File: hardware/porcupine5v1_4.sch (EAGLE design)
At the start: 45 parts, among them X1 PROGCON

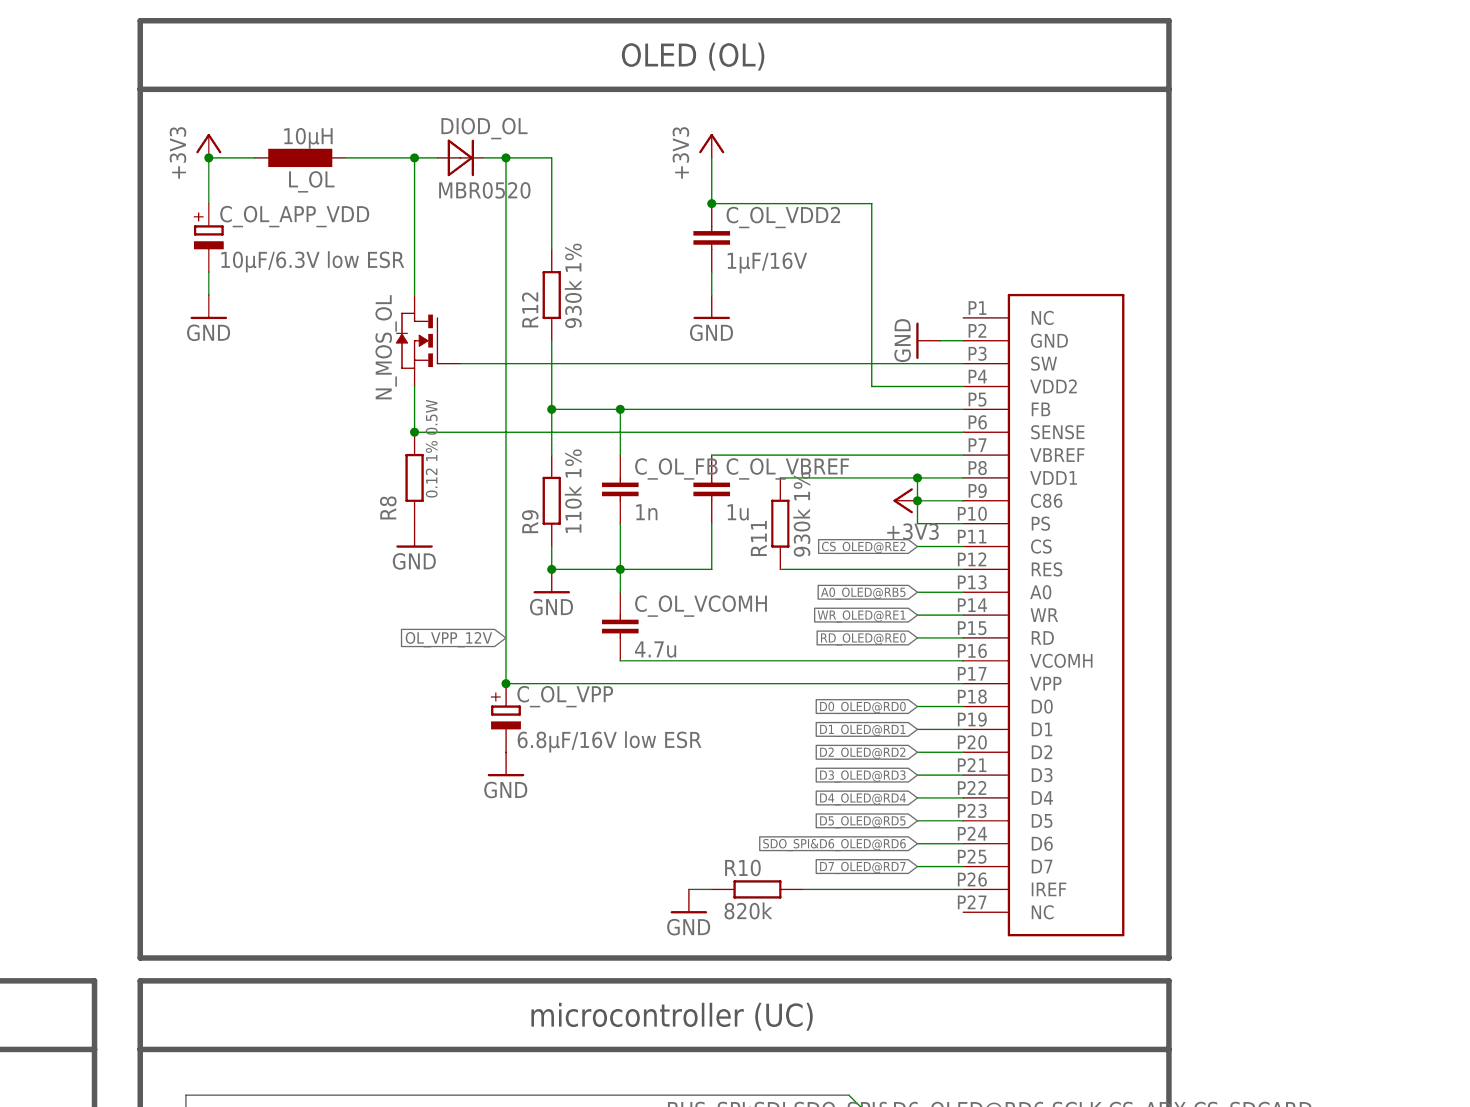
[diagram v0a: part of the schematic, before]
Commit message: added new OLEDdisplay
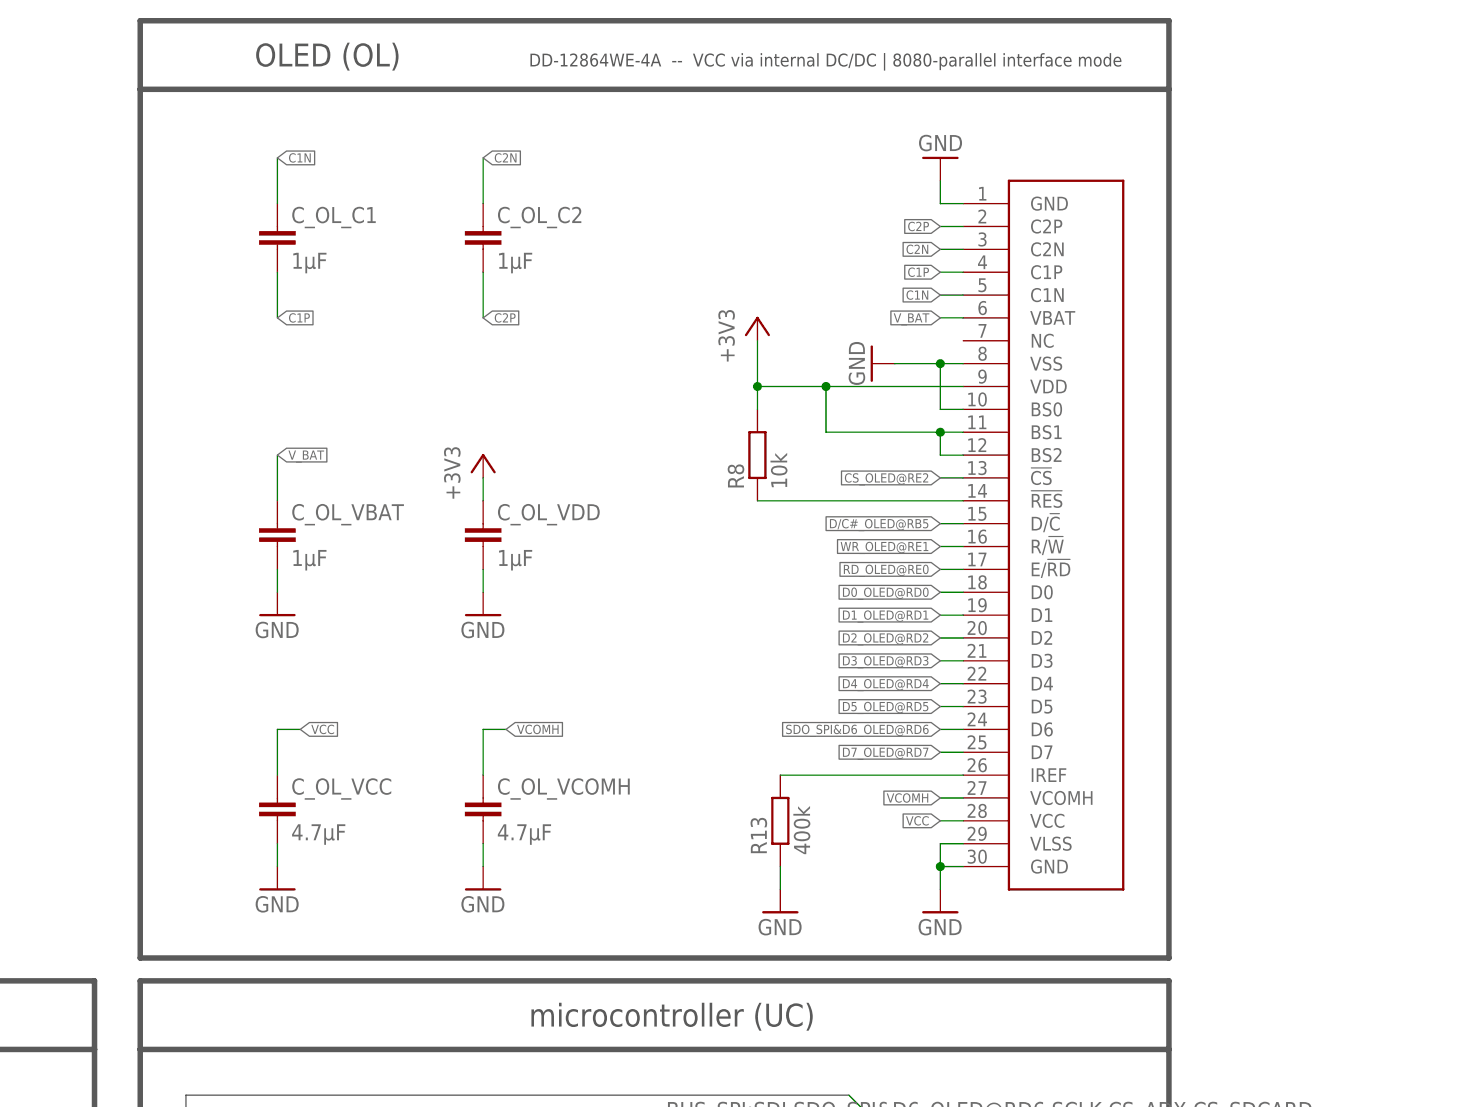
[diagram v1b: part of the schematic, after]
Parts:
- removed CON_OLED: OLED_DENSITRON, HedgehogLib:OLED_DENSITRON
- removed C_OL_APP_VDD: 10µF/6.3V low ESR, rcl:CPOL-EUA/3216-18R
- removed C_OL_FB: 1n, rcl:C-EUC0603K
- removed C_OL_VBREF: 1u, rcl:C-EUC0603K
- removed C_OL_VDD2: 1µF/16V, rcl:C-EUC0603K
- removed C_OL_VPP: 6.8µF/16V low ESR, rcl:CPOL-EUA/3216-18R
- removed DIOD_OL: MBR0520, HedgehogLib:MBR0520
- removed L_OL: 10µH, HedgehogLib:LQH3NP
- removed N_MOS_OL: (no value), HedgehogLib:MGSF1N02LT1
- removed R10: 820k, rcl:R-EU_R0603
- removed R11, R12: 930k 1%, rcl:R-EU_R0603
- removed R9: 110k 1%, rcl:R-EU_R0603
- added C_OL_C1, C_OL_C2, C_OL_VBAT, C_OL_VDD: 1µF, rcl:C-EUC0603K
- added C_OL_VCC: 4.7µF, rcl:C-EUC0603K
- added R13: 400k, rcl:R-EU_R0603
- added U$1: DD-12864WE-4A, HedgehogLib:DD-12864WE-4A
- C_OL_VCOMH: value 4.7u -> 4.7µF
- R8: value 0.12 1% 0.5W -> 10k; device HedgehogLib:RESISTOR_PAN_ERJB3CFR12V -> rcl:R-EU_R0603
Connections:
- removed net N$10: DIOD_OL.A, L_OL.2, N_MOS_OL.D
- removed net OL_FB: CON_OLED.FB, C_OL_FB.1, R12.1, R9.2
- removed net OL_IREF: CON_OLED.IREF, R10.2
- removed net OL_SENSE: CON_OLED.SENSE, N_MOS_OL.S, R8.2
- removed net OL_SW: CON_OLED.SW, N_MOS_OL.G
- removed net OL_VBREF: CON_OLED.VBREF, C_OL_VBREF.1
- removed net OL_VCOMH: CON_OLED.VCOMH, C_OL_VCOMH.2
- removed net OL_VPP_12V: CON_OLED.VPP, C_OL_VPP.+, DIOD_OL.C, R12.2
- new net C1N: C_OL_C1.1, U$1.C1N
- new net C1P: C_OL_C1.2, U$1.C1P
- new net C2N: C_OL_C2.1, U$1.C2N
- new net C2P: C_OL_C2.2, U$1.C2P
- new net D/C#_OLED@RB5: U$1.D/!C
- new net VCC: C_OL_VCC.1, U$1.VCC
- new net VCOMH: C_OL_VCOMH.1, U$1.VCOMH
- net +3V3: now also C_OL_VDD.1, R8.2, U$1.BS1, U$1.BS2, U$1.VDD; no longer CON_OLED.C86, CON_OLED.PS, CON_OLED.VDD1, CON_OLED.VDD2, C_OL_APP_VDD.+, C_OL_VDD2.2, L_OL.1, R11.2
- net A0_OLED@RB5: no longer CON_OLED.A0
- net CS_OLED@RE2: now also U$1.!CS; no longer CON_OLED.CS
- net D0_OLED@RD0: now also U$1.D0; no longer CON_OLED.D0
- net D1_OLED@RD1: now also U$1.D1; no longer CON_OLED.D1
- net D2_OLED@RD2: now also U$1.D2; no longer CON_OLED.D2
- net D3_OLED@RD3: now also U$1.D3; no longer CON_OLED.D3
- net D4_OLED@RD4: now also U$1.D4; no longer CON_OLED.D4
- net D5_OLED@RD5: now also U$1.D5; no longer CON_OLED.D5
- net D7_OLED@RD7: now also R13.2, U$1.D7, U$1.IREF; no longer CON_OLED.D7
- net GND: now also C_OL_VBAT.2, C_OL_VCC.2, C_OL_VCOMH.2, C_OL_VDD.2, R13.1, U$1.BS0, U$1.GND@1, U$1.GND@30, U$1.VLSS, U$1.VSS; no longer CON_OLED.GND, C_OL_APP_VDD.-, C_OL_FB.2, C_OL_VBREF.2, C_OL_VCOMH.1, C_OL_VDD2.1, C_OL_VPP.-, R10.1, R8.1, R9.1
- net RD_OLED@RE0: now also U$1.E/!RD; no longer CON_OLED.RD
- net RES_OLED: now also R8.1, U$1.!RES; no longer CON_OLED.RES, R11.1
- net SDO_SPI&D6_OLED@RD6: now also U$1.D6; no longer CON_OLED.D6
- net V_BAT: now also C_OL_VBAT.1, U$1.VBAT
- net WR_OLED@RE1: now also U$1.R/!W; no longer CON_OLED.WR
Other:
- note added: "DD-12864WE-4A -- VCC via internal DC/DC | 8080-parallel interface mode"
- moved on the sheet: C_OL_VCOMH, R8

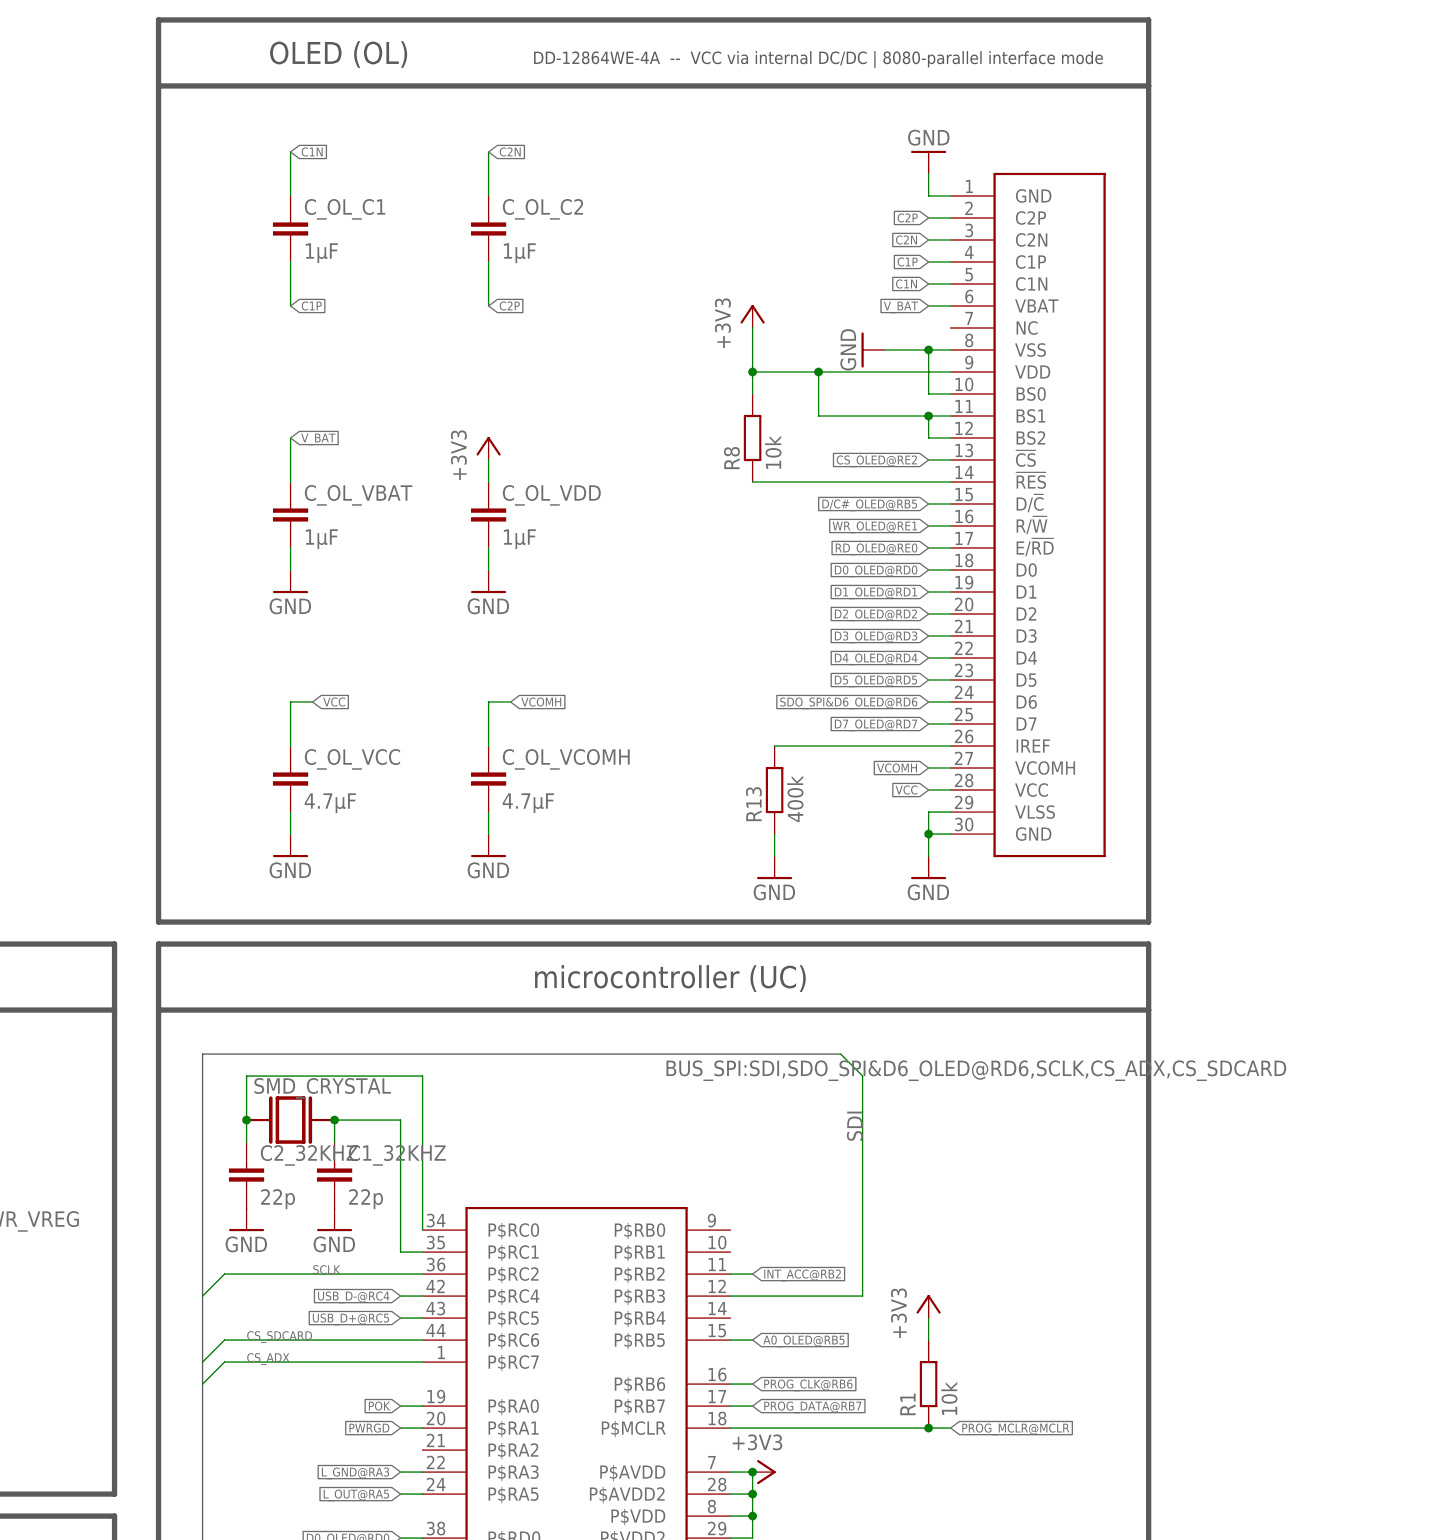
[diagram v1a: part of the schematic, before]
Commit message: updated new OLED 5.1.4 version
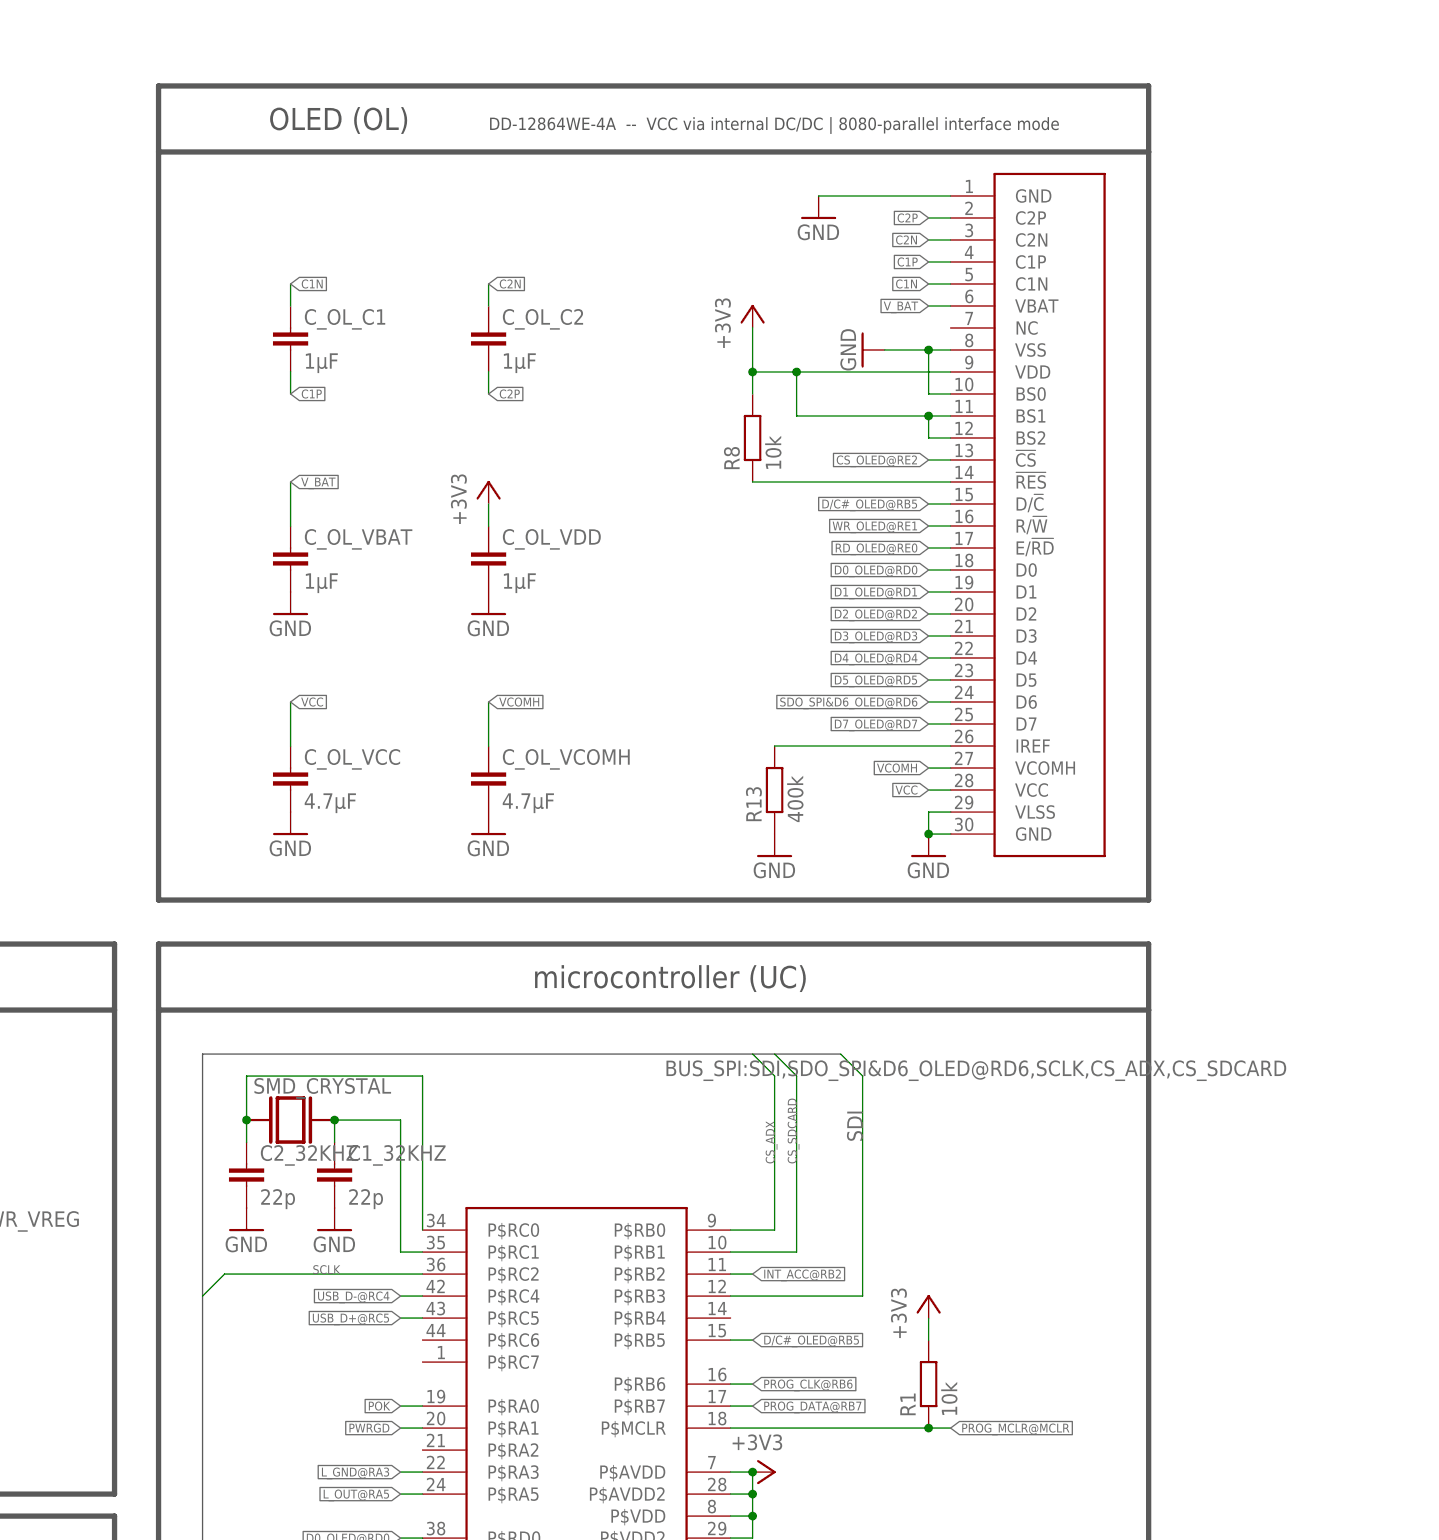
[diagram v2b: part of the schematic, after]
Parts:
- renumbered U$1 to OLED
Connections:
- removed net A0_OLED@RB5: PIC_CONTROLLER.P$RB5
- new net IREF: OLED.IREF, R13.2
- net CS_ADX: now also PIC_CONTROLLER.P$RB0; no longer PIC_CONTROLLER.P$RC7
- net CS_SDCARD: now also PIC_CONTROLLER.P$RB1; no longer PIC_CONTROLLER.P$RC6
- net D/C#_OLED@RB5: now also PIC_CONTROLLER.P$RB5
- net D7_OLED@RD7: no longer OLED.IREF, R13.2
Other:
- moved on the sheet: C_OL_C1, C_OL_C2, C_OL_VBAT, C_OL_VDD
